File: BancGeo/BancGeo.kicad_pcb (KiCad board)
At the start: 2 copper layers, 97 parts, among them P1 Alim, P2 Batt, P3 CONN_01X05, P4 Capt1, P5 Capt2, P6 Capt3, P7 Capt4, Q1 2N7002E, Q2 PMV37EN2R, Q3 PMV37EN2R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

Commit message: Update Bancgeo
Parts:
- added D2: SSA33L-E3, Yame_library:DO-214AC, F.Cu at (198.9, 85.6)
- added P8: USB_D-, Yame_library:Test_SMT, F.Cu at (200.6, 60.8)
- added P9: USB_D+, Yame_library:Test_SMT, F.Cu at (198.2, 72.2)
- added SW1: Switch_DPST, Yame_library:Switch_EVQP0, F.Cu at (174.2, 84.8)
- added SW2: SW_PUSH, Yame_library:SW_BancGeo, F.Cu at (207.6, 51.5)
- added T1: DRQ127-100-R, Yame_library:DRQ127_CPL_TR, F.Cu at (219.5, 62.5)
- added U11: HM-10_BLE_Module, Yame_library:HM-10_BLE, F.Cu at (171.9, 48.1)
- moved Q2 83.9 mm to (241.2, 48.9)
- moved P2 83.1 mm to (236.0, 52.1)
- moved C22 75.0 mm to (240.6, 55.3)
- moved Q3 69.6 mm to (241.2, 52.5)
- moved U6 69.4 mm to (225.5, 51.5)
- moved C9 69.0 mm to (188.3, 88.0)
- moved C26 69.0 mm to (191.8, 88.0)
- moved C27 66.5 mm to (205.6, 60.6)
- moved U5 66.0 mm to (201.6, 57.8)
- moved C4 65.9 mm to (209.1, 60.6)
- moved C32 65.4 mm to (240.1, 67.0)
- moved D4 64.9 mm to (181.0, 82.4)
- moved C7 64.7 mm to (184.7, 88.0)
- moved D1 64.3 mm to (209.1, 57.8)
- moved U2 62.4 mm to (192.1, 85.2)
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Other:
- board outline added: 127.5 x 96.5 mm

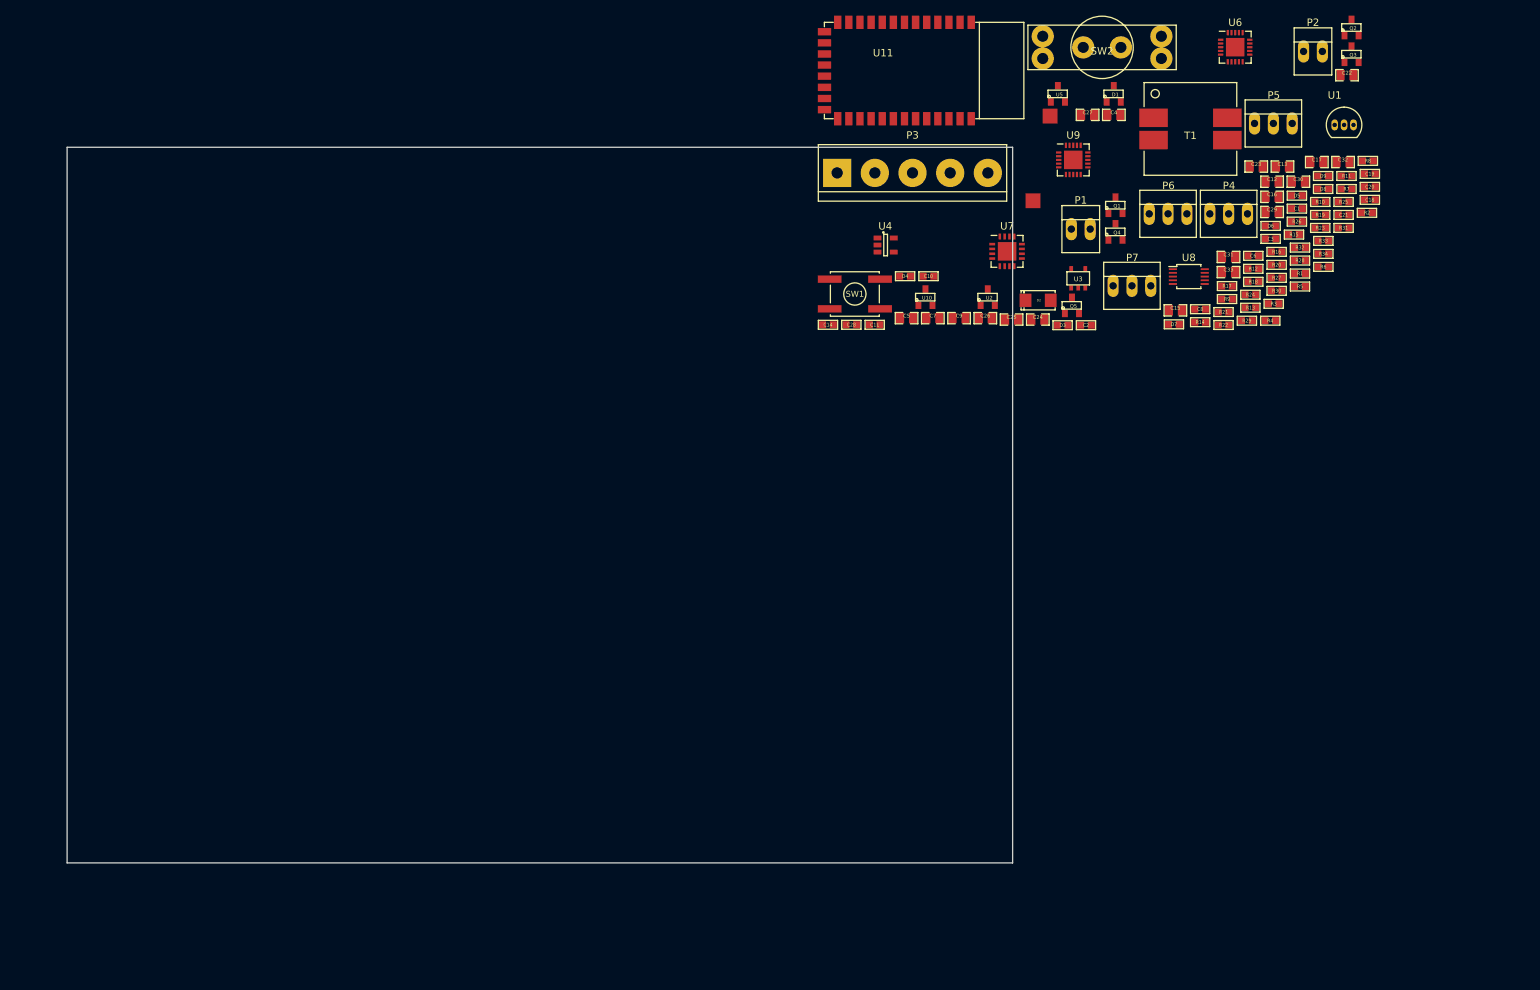
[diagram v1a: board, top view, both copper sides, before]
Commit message: update bancgeo
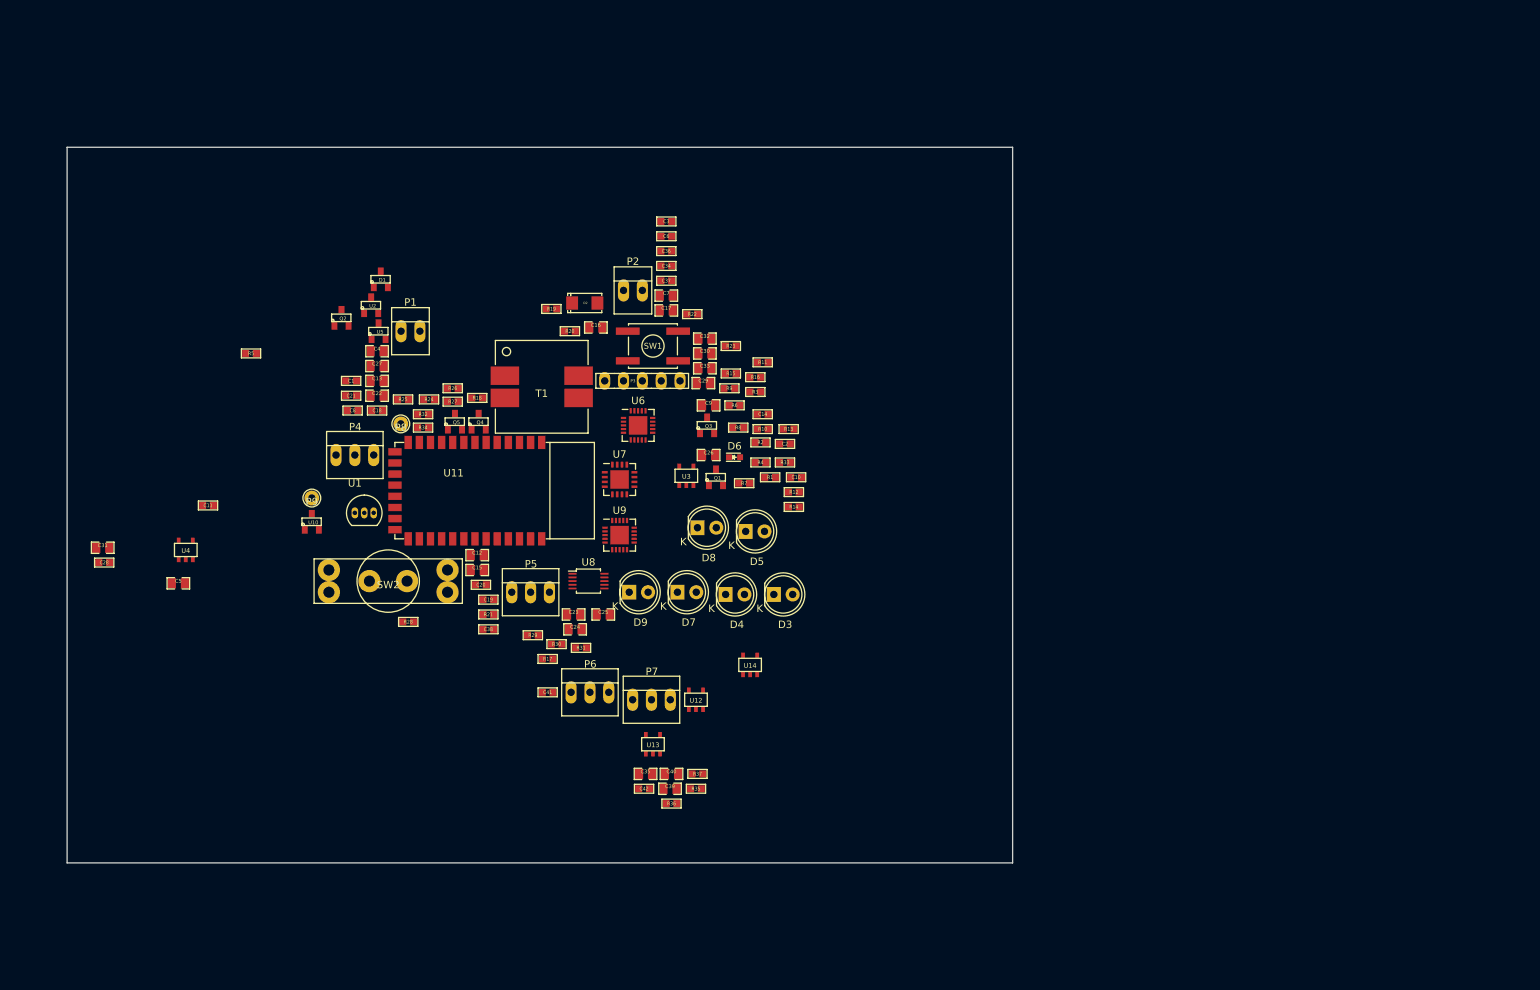
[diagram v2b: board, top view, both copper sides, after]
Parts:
- added C34: 100n, Yame_library:SM0603-MR, F.Cu at (148.8, 81.0)
- added C35: 1u, Yame_library:SM0805-MR, F.Cu at (146.0, 149.5)
- added C36: 100n, Yame_library:SM0603-MR, F.Cu at (148.8, 79.0)
- added C37: 100n, Yame_library:SM0603-MR, F.Cu at (148.8, 83.0)
- added C38: 100n, Yame_library:SM0603-MR, F.Cu at (124.8, 130.0)
- added C39: 1u, Yame_library:SM0805-MR, F.Cu at (149.3, 151.5)
- added C40: 1u, Yame_library:SM0805-MR, F.Cu at (149.5, 149.5)
- added C41: 100n, Yame_library:SM0603-MR, F.Cu at (132.8, 138.5)
- added C42: 100n, Yame_library:SM0603-MR, F.Cu at (145.8, 151.5)
- added R35: 10, Yame_library:SM0603-MR, F.Cu at (152.8, 151.5)
- added R36: 10, Yame_library:SM0603-MR, F.Cu at (149.5, 153.5)
- added R37: 10, Yame_library:SM0603-MR, F.Cu at (153.0, 149.5)
- added U12: LM4120IM5X-5.0/NOPB, Yame_library:SOT23-5-MR, F.Cu at (152.8, 139.5)
- added U13: LM4120IM5X-5.0/NOPB, Yame_library:SOT23-5-MR, F.Cu at (147.0, 145.5)
- added U14: LM4120IM5X-5.0/NOPB, Yame_library:SOT23-5-MR, F.Cu at (160.1, 134.8)
- D3, D4, D5, D7, D8, D9: footprint Yame_library:SM0603-MR -> LEDs:LED-5MM
- D6: footprint Yame_library:SM0603-MR -> LEDs:LED_0603
- P3: footprint Connect:bornier5 -> Yame_library:HE10_14-5C-2.54-MR
- P8, P9: footprint Yame_library:Test_SMT -> Yame_library:Test_Point_T_H
- U4: footprint TO_SOT_Packages_SMD:SOT-23-5 -> Yame_library:SOT23-5-MR
- moved C31 156.8 mm to (72.8, 119.0)
- moved U1 142.1 mm to (106.8, 114.3)
- moved R5 141.7 mm to (92.8, 92.8)
- moved Q2 141.7 mm to (105.0, 88.0)
- moved C22 137.7 mm to (109.8, 98.5)
- moved C18 136.9 mm to (109.8, 100.5)
- moved C21 136.0 mm to (106.3, 98.5)
- moved C19 132.0 mm to (124.8, 126.0)
- moved C20 131.3 mm to (123.8, 124.0)
- moved R28 129.7 mm to (114.0, 129.0)
- moved C1 129.6 mm to (106.3, 96.5)
- moved R25 129.6 mm to (113.3, 99.0)
- moved C13 125.5 mm to (109.8, 96.5)
- moved R34 123.6 mm to (116.0, 102.8)
- moved P4 122.2 mm to (106.8, 106.5)
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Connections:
- C11 pad 1: /+Vref -> /+Vref1
- C7 pad 1: Net-(C7-Pad1) -> /+Vbat
- P4 pad 1: /+Vref -> /+Vref1
- P5 pad 1: /+Vref -> /+Vref2
- P6 pad 1: /+Vref -> /+Vref3
- P7 pad 1: /+Vref -> /+Vref4
- U4 pad 5: /+Vref -> /+Vref1
- U5 pad 3: Net-(C7-Pad1) -> /+Vbat

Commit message: Update BancGeo
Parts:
- removed D1: MMBD6100LT1G, Yame_library:SOT23-MR
- added R38, R39, R40, R41, R42, R43: 470, Yame_library:SM0603-MR, F.Cu at (131.8, 171.6)
- added REF**: Metal_4.5_6, Yame_library:Metal_4.5_6, F.Cu at (191.1, 100.7)
- added REF**: Metal_4.5_6, Yame_library:Metal_4.5_6, F.Cu at (72.8, 100.8)
- SW1: value Switch_DPST -> SWITCH_BRIDE; footprint Yame_library:Switch_EVQP0 -> SWITCH_BRIDE
- SW2: footprint Yame_library:SW_BancGeo -> Buttons_Switches_SMD:SW_SPST_B3U-1000P
- U12, U13, U14, U4: footprint Yame_library:SOT23-5-MR -> TO_SOT_Packages_SMD:SOT-23-5
- moved P5 127.5 mm to (248.4, 173.4)
- moved P4 104.5 mm to (187.9, 172.4)
- moved P7 82.5 mm to (222.3, 172.8)
- moved U1 81.1 mm to (186.2, 130.5)
- moved C10 81.1 mm to (245.8, 125.7)
- moved C11 81.1 mm to (166.4, 129.5)
- moved P9 81.1 mm to (180.4, 128.5)
- moved R1 81.1 mm to (242.2, 125.7)
- moved R12 81.1 mm to (245.4, 127.7)
- moved R7 81.1 mm to (238.8, 126.5)
- moved U14 81.1 mm to (239.6, 151.0)
- moved U4 81.1 mm to (163.4, 135.5)
- moved U9 81.1 mm to (221.9, 133.5)
- moved C12 81.1 mm to (202.8, 136.2)
- moved C15 81.1 mm to (202.8, 138.2)
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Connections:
- P5 pad 1: /+Vref2 -> /+Vref1
- P6 pad 1: /+Vref3 -> /+Vref2
- P7 pad 1: /+Vref4 -> /+Vref2
- SW1 pad 3: Net-(R22-Pad1) -> GND
- U9 pad 10: Net-(D4-Pad2) -> Net-(R38-Pad2)
- U9 pad 11: Net-(D5-Pad2) -> Net-(R42-Pad2)
- U9 pad 12: Net-(D7-Pad2) -> Net-(R39-Pad2)
- U9 pad 13: Net-(D8-Pad2) -> Net-(R43-Pad2)
- U9 pad 14: Net-(D9-Pad2) -> Net-(R40-Pad2)
- U9 pad 9: Net-(D3-Pad2) -> Net-(R41-Pad2)

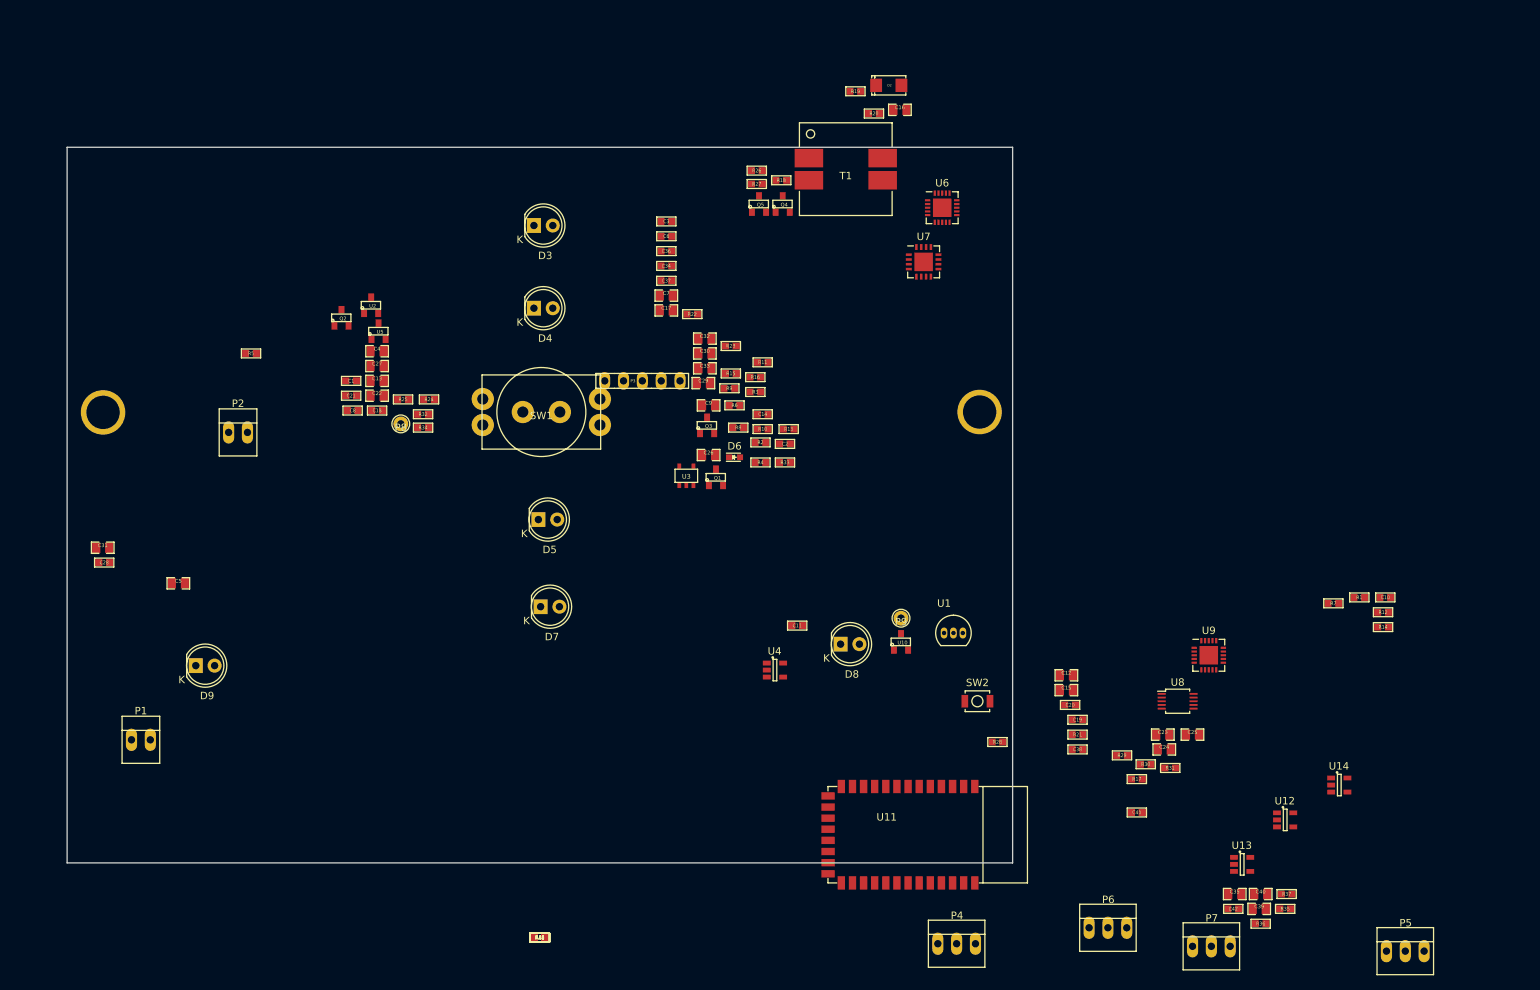
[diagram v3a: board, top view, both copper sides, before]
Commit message: place and lock components
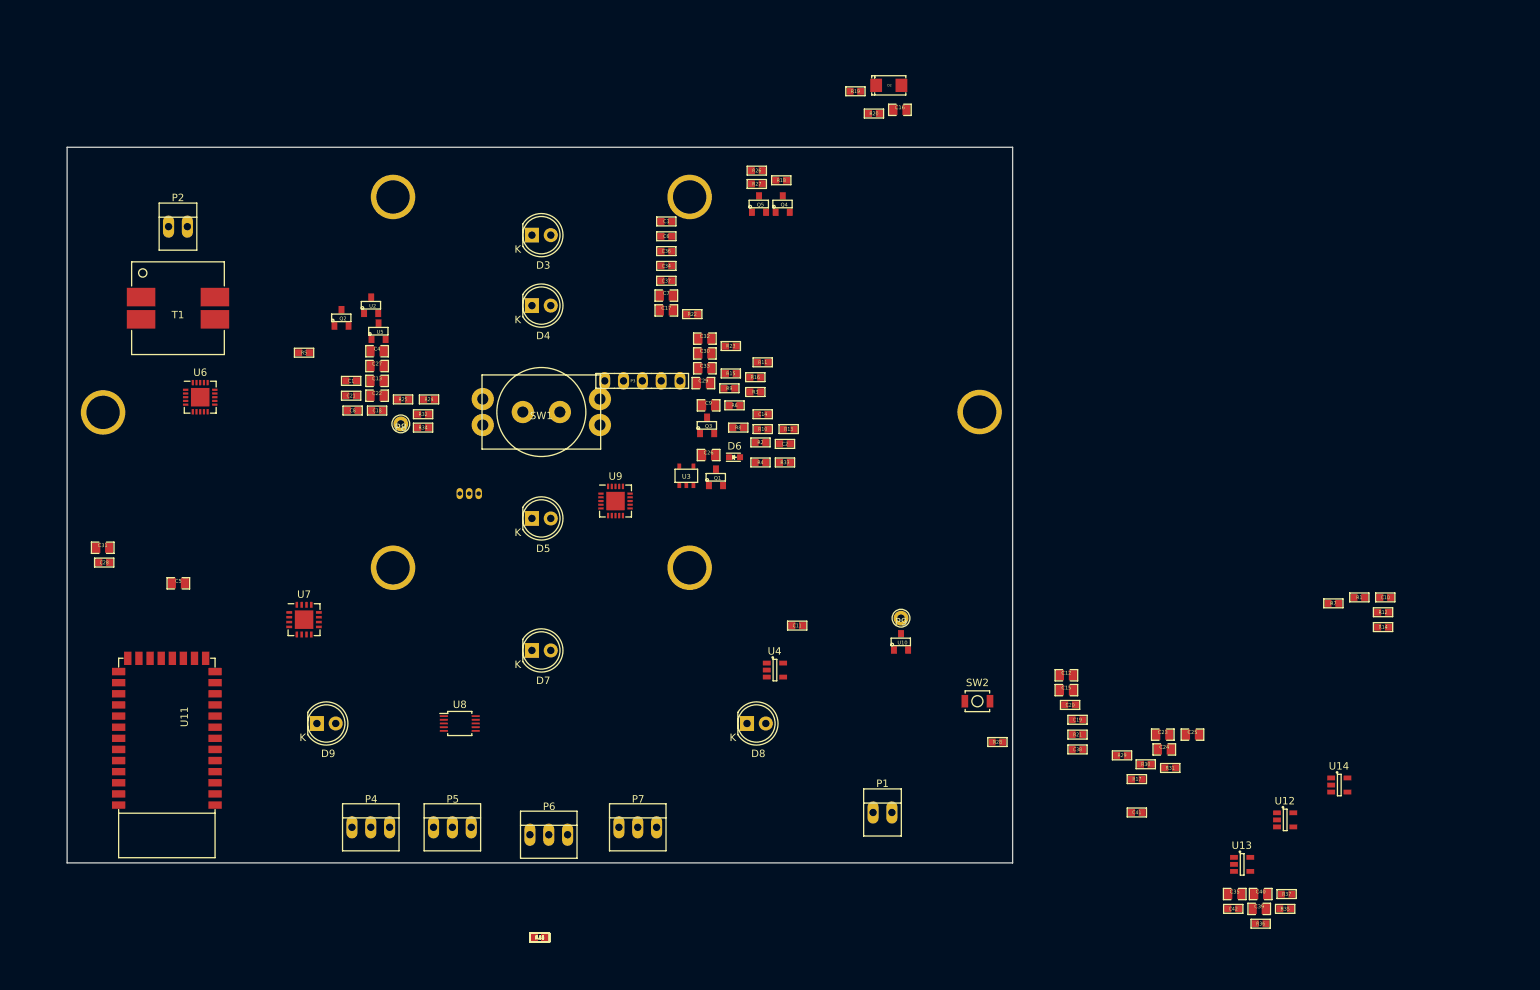
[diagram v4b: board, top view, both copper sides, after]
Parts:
- added REF**: Metal_4.5_6, Yame_library:Metal_4.5_6, F.Cu at (112.0, 71.7)
- added REF**: Metal_4.5_6, Yame_library:Metal_4.5_6, F.Cu at (151.9, 71.7)
- added REF**: Metal_4.5_6, Yame_library:Metal_4.5_6, F.Cu at (112.0, 121.7)
- added REF**: Metal_4.5_6, Yame_library:Metal_4.5_6, F.Cu at (151.9, 121.7)
- D3, D4, D5, D7, D8, D9: footprint LEDs:LED-5MM -> Yame_library:LED-5MM_center
- U1: moved to B.Cu
- moved P5 129.6 mm to (120.0, 156.7)
- moved U6 103.3 mm to (86.0, 98.7)
- moved P1 100.5 mm to (177.9, 154.7)
- moved U8 96.8 mm to (121.0, 142.7)
- moved U7 96.5 mm to (100.0, 128.7)
- moved T1 92.0 mm to (83.0, 86.7)
- moved U11 85.9 mm to (88.0, 135.7), turned to 270 degrees
- moved U9 82.7 mm to (141.9, 112.7)
- moved P4 80.5 mm to (109.0, 156.7)
- moved P7 79.0 mm to (144.9, 156.7)
- moved P6 76.4 mm to (132.9, 157.7)
- moved U1 68.0 mm to (121.0, 111.7)
- moved P2 28.9 mm to (83.0, 75.7)
- moved D9 19.3 mm to (103.0, 142.7)
- moved D8 15.6 mm to (160.9, 142.7)
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
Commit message: Update Bancgeo
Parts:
- removed C36, C37, C41, C42: 100n, Yame_library:SM0603-MR
- removed C40: 1u, Yame_library:SM0805-MR
- removed R36, R37: 10, Yame_library:SM0603-MR
- removed the REF** at (151.9, 121.7)
- removed U13, U14: LM4120IM5X-5.0/NOPB, TO_SOT_Packages_SMD:SOT-23-5
- D3, D4, D5, D7, D8, D9: footprint Yame_library:LED-5MM_center -> LEDs:LED-5MM
- U1: footprint TO_SOT_Packages_THT:TO-92_Inline_Narrow_Oval -> Yame_library:SOT23-MR
- moved C10 139.0 mm to (106.8, 129.1)
- moved R7 134.3 mm to (104.5, 129.8), turned to 270 degrees
- moved R1 129.7 mm to (112.8, 116.3)
- moved SW2 129.0 mm to (63.1, 121.3)
- moved U6 107.2 mm to (188.6, 129.9), turned to 180 degrees
- moved P9 106.8 mm to (73.7, 130.4)
- moved T1 105.9 mm to (175.4, 138.2), turned to 90 degrees
- moved C23 104.9 mm to (111.0, 149.5)
- moved P2 101.5 mm to (178.2, 110.6)
- moved C4 91.3 mm to (192.7, 130.9), turned to 270 degrees
- moved C24 90.2 mm to (125.8, 149.6)
- moved R35 86.4 mm to (147.3, 151.9), turned to 180 degrees
- moved U12 85.5 mm to (147.1, 149.0)
- moved R29 85.4 mm to (125.0, 151.9), turned to 90 degrees
- moved U10 85.1 mm to (95.8, 140.2)
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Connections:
- C12 pad 1: Net-(C12-Pad1) -> /+12v
- C15 pad 1: Net-(C12-Pad1) -> /+12v
- C29 pad 1: /+Vref -> /+Vref1
- C30 pad 1: /+Vref -> /+Vref2
- C32 pad 1: /+Vref -> /+Vref1
- C33 pad 1: /+Vref -> /+Vref2
- R3 pad 1: /+Vref -> /+Vref1
- R9 pad 2: /+Vref -> /+Vref1
- T1 pad 1: Net-(C12-Pad1) -> /+12v

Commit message: Update Bancgeo
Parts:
- removed C39: 1u, Yame_library:SM0805-MR
- added R36: nc, Yame_library:SM0603-MR, F.Cu at (133.9, 146.8)
- added REF**: Metal_4.5_6, Yame_library:Metal_4.5_6, F.Cu at (151.9, 121.7)
- D3, D4, D5, D7, D8, D9: footprint LEDs:LED-5MM -> Yame_library:LED-5MM_center
- moved R26 109.5 mm to (93.5, 154.3), turned to 270 degrees
- moved Q4 106.4 mm to (96.3, 154.3), turned to 270 degrees
- moved R27 104.8 mm to (93.5, 150.1), turned to 270 degrees
- moved C20 104.5 mm to (100.3, 122.2)
- moved Q5 101.1 mm to (96.3, 150.1), turned to 270 degrees
- moved R17 99.9 mm to (113.4, 135.6)
- moved R33 98.2 mm to (71.7, 138.7), turned to 180 degrees
- moved R41 94.8 mm to (137.9, 76.8)
- moved R38 85.3 mm to (137.9, 86.3)
- moved R24 67.9 mm to (99.0, 155.1), turned to 90 degrees
- moved R23 64.1 mm to (98.8, 117.7)
- moved R25 62.9 mm to (99.0, 150.8), turned to 90 degrees
- moved R22 61.9 mm to (99.6, 120.0), turned to 270 degrees
- moved C27 58.2 mm to (96.3, 141.3)
- moved R42 56.7 mm to (137.9, 115.0)
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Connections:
- U9 pad 10: Net-(R38-Pad2) -> Net-(R43-Pad2)
- U9 pad 11: Net-(R42-Pad2) -> /SetPreChg
- U9 pad 12: Net-(R39-Pad2) -> /SetTail
- U9 pad 13: Net-(R43-Pad2) -> Net-(R41-Pad2)
- U9 pad 14: Net-(R40-Pad2) -> Net-(R38-Pad2)
- U9 pad 15: /SetPreChg -> Net-(R42-Pad2)
- U9 pad 16: /SetTail -> Net-(R40-Pad2)
- U9 pad 9: Net-(R41-Pad2) -> Net-(R39-Pad2)
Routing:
- net /+Vref1: track 0.00 -> 83.1 mm, vias 0 -> 8
- net Net-(R41-Pad2): track 0.00 -> 58.1 mm
- net Net-(R38-Pad2): track 0.00 -> 46.3 mm
- net Net-(R40-Pad2): track 0.00 -> 39.0 mm
- net Net-(R43-Pad2): track 0.00 -> 37.3 mm
- net /+Vbat: track 0.00 -> 37.2 mm
- net Net-(C23-Pad1): track 0.00 -> 28.0 mm
- net /Rx_µC: track 0.00 -> 27.9 mm
- net /+5V: track 0.00 -> 27.4 mm, vias 0 -> 2
- net /Tx_µC: track 0.00 -> 26.1 mm, vias 0 -> 2
- net Net-(C26-Pad1): track 0.00 -> 25.7 mm
- net /+3.3V: track 0.00 -> 16.0 mm
- net Net-(Q2-Pad1): track 0.00 -> 13.5 mm
- net Net-(R42-Pad2): track 0.00 -> 12.7 mm
- net Net-(C24-Pad1): track 0.00 -> 12.4 mm
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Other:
- rule via_min_drill: 0.3 -> 0.35
- rule via_min_size: 0.4 -> 0.6
